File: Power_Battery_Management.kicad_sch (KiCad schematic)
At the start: 19 parts, among them J501 S2B-PH-SM4-TB, Q501 CSD85302L, U501 BQ29737DSER, U502 MCP73831T-2ACI/MC

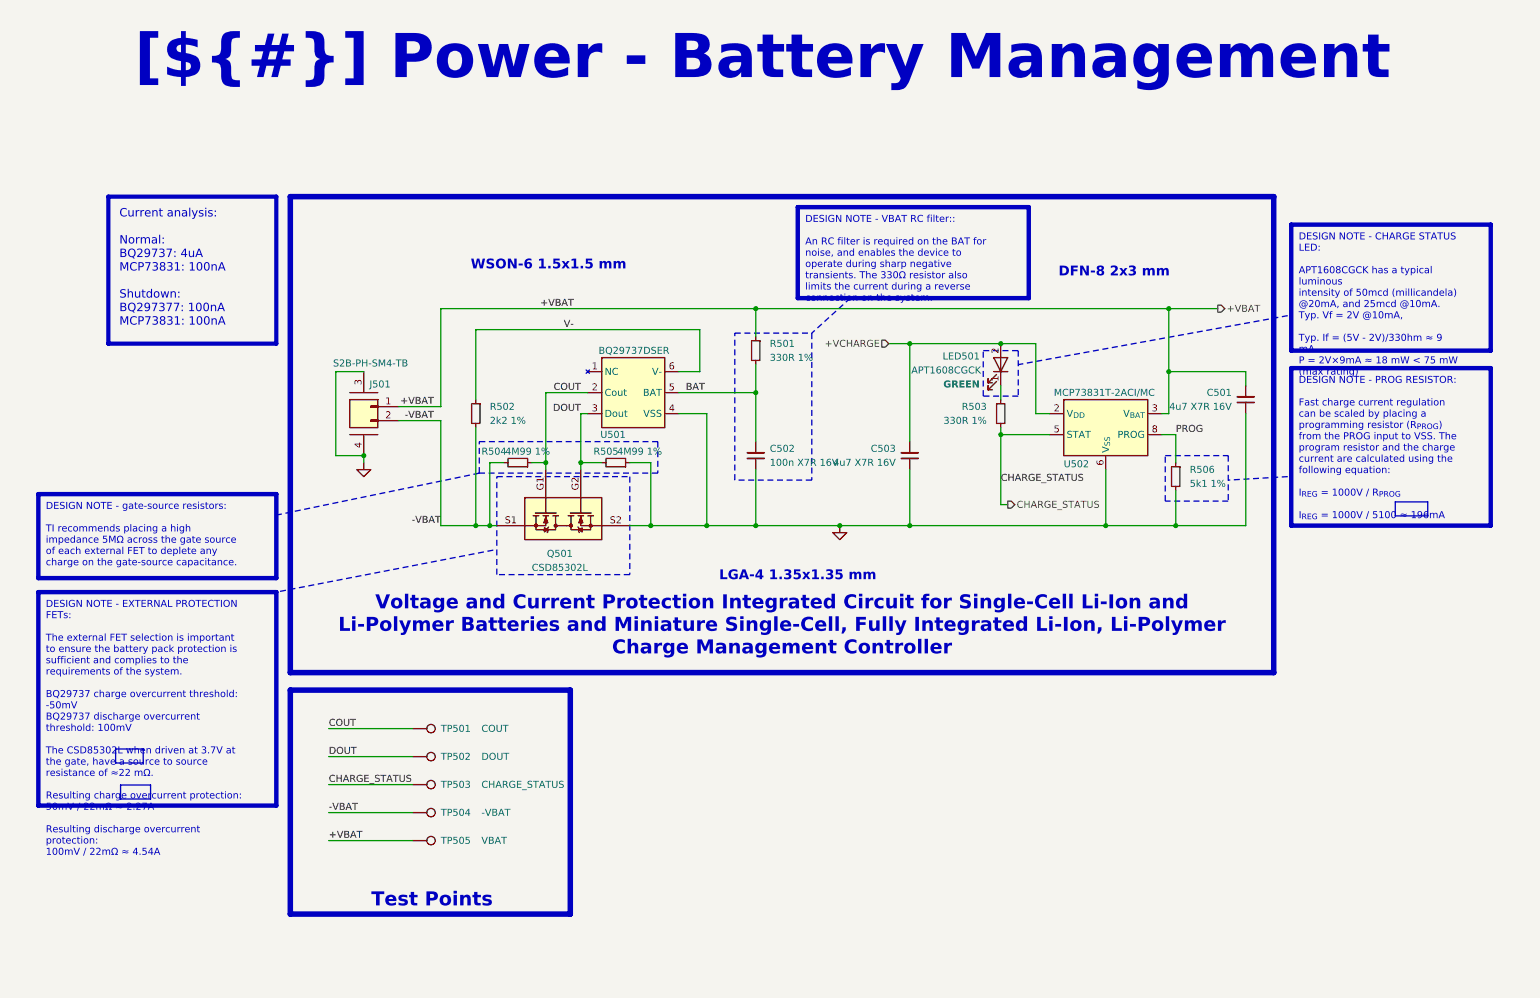
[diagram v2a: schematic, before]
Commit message: Finished schematic, imported all footprints, all 3D models and created STM32 project, now need to proofread shematic before layout
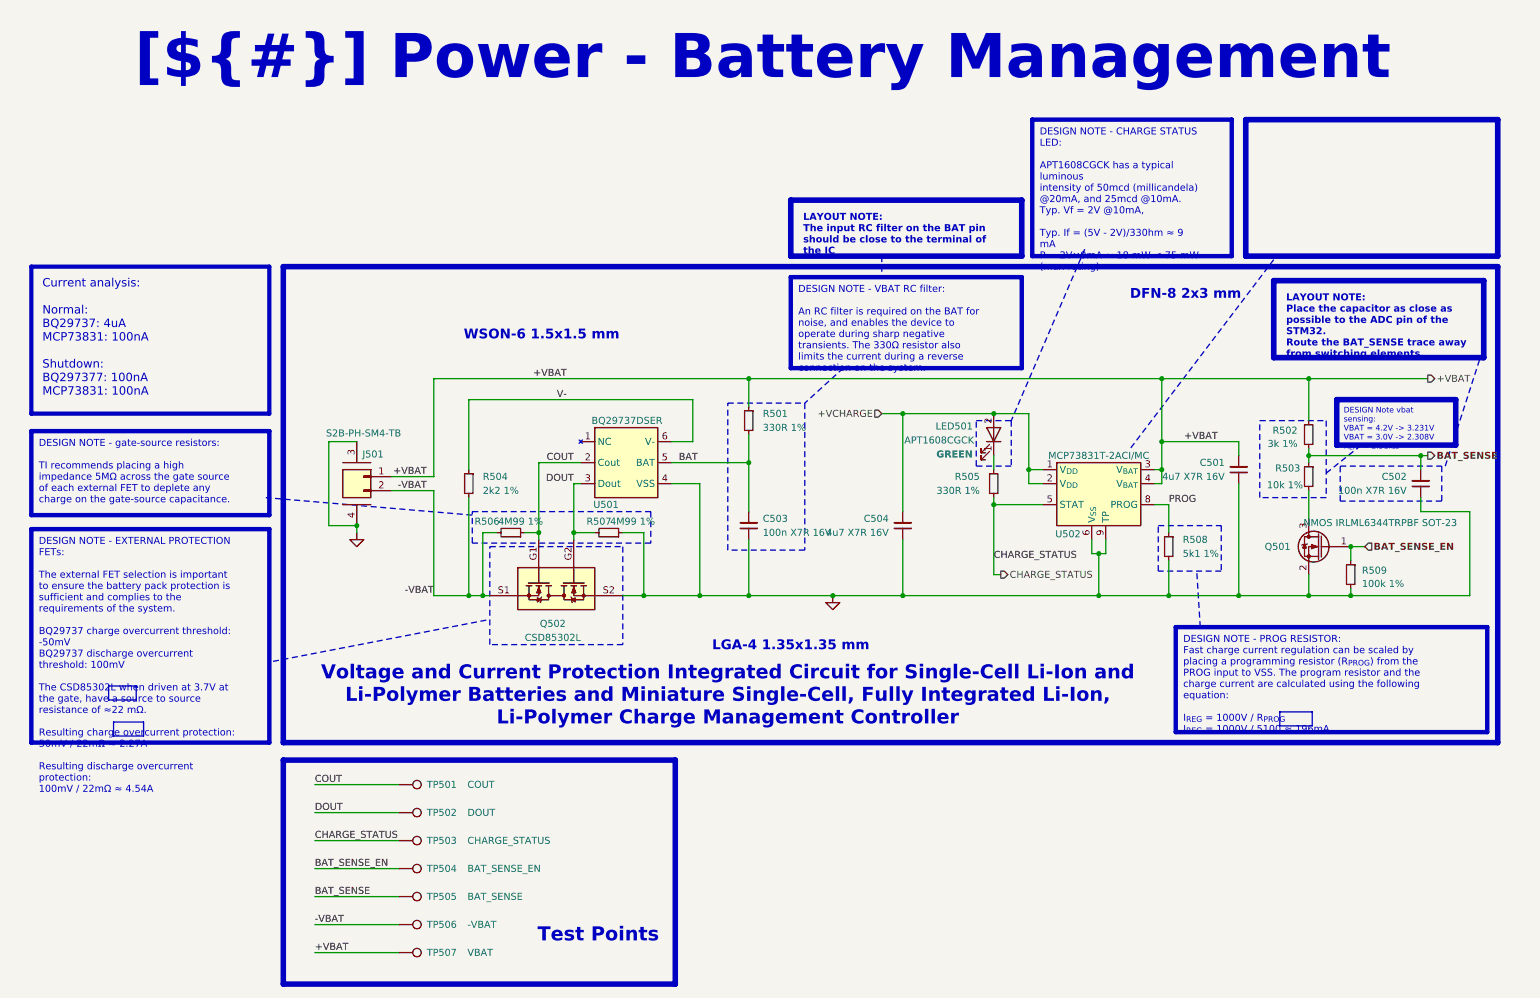
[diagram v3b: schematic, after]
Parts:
- added C502: 100n X7R 16V, Capacitor_SMD:C_0402_1005Metric, symbol Device:C_Small
- added Q501: NMOS IRLML6344TRPBF SOT-23, Package_TO_SOT_SMD:SOT-23, symbol Transistor_FET_Other:Q_NMOS_Depletion_GSD
- added R502: 3k 1%, Resistor_SMD:R_0402_1005Metric, symbol Device:R_Small
- added R503: 10k 1%, Resistor_SMD:R_0402_1005Metric, symbol Device:R_Small
- added R509: 100k 1%, Resistor_SMD:R_0402_1005Metric, symbol Device:R_Small
- added TP504: BAT_SENSE_EN, 0_Plume:TestPoint_Pad_D0.5mm_Back, symbol Connector:TestPoint
- added TP505: BAT_SENSE, 0_Plume:TestPoint_Pad_D0.5mm_Back, symbol Connector:TestPoint
- renumbered C502 to C503, C503 to C504, Q501 to Q502, R502 to R504, R503 to R505, R504 to R506, R505 to R507, R506 to R508, TP504 to TP506, TP505 to TP507
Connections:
- net +VBAT: now also R502.1
- net +VCHARGE: now also U502.1 (V_{DD})
- net GND: now also U502.9 (TP), C502.1, Q501.2 (S), R509.2
- new net: Q501.3 (D), R503.2
- new net BAT_SENSE: C502.2, R502.2, R503.1, TP505.1
- new net BAT_SENSE_EN: Q501.1 (G), R509.1, TP504.1
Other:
- moved on the sheet: C501, C503, C504, J501, LED501, Q502, R501, R504, R505, R506, R507, R508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

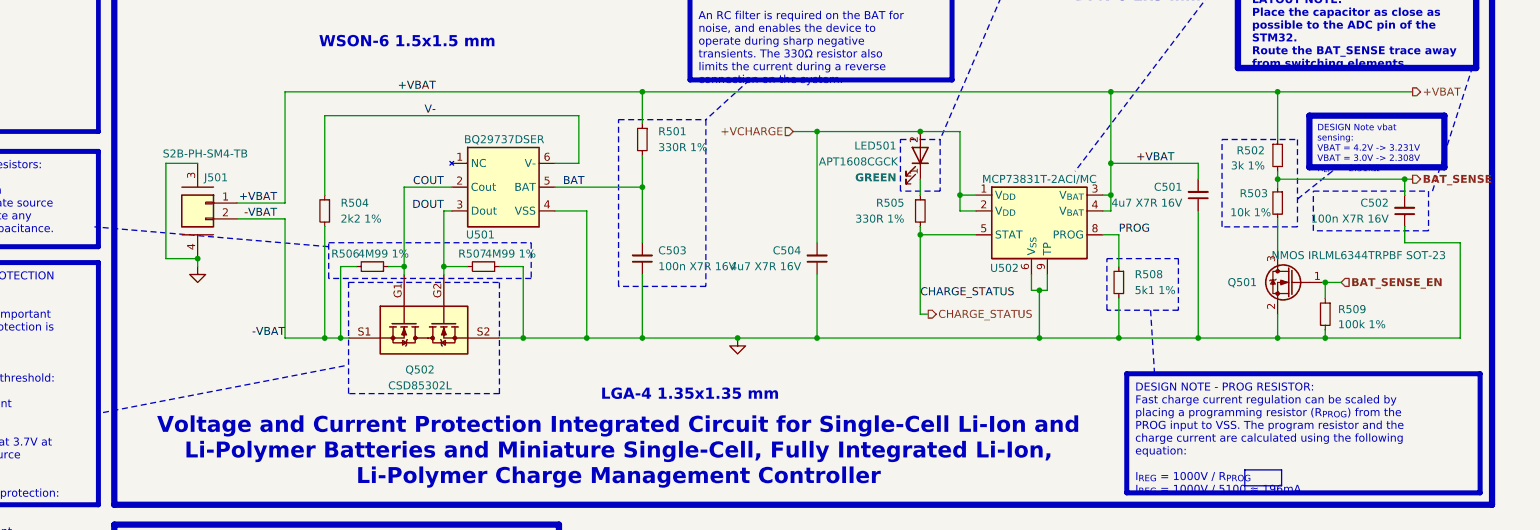
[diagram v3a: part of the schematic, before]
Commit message: Reviewed shematic, cleaned all DRC errors, chosed stackup, started layout
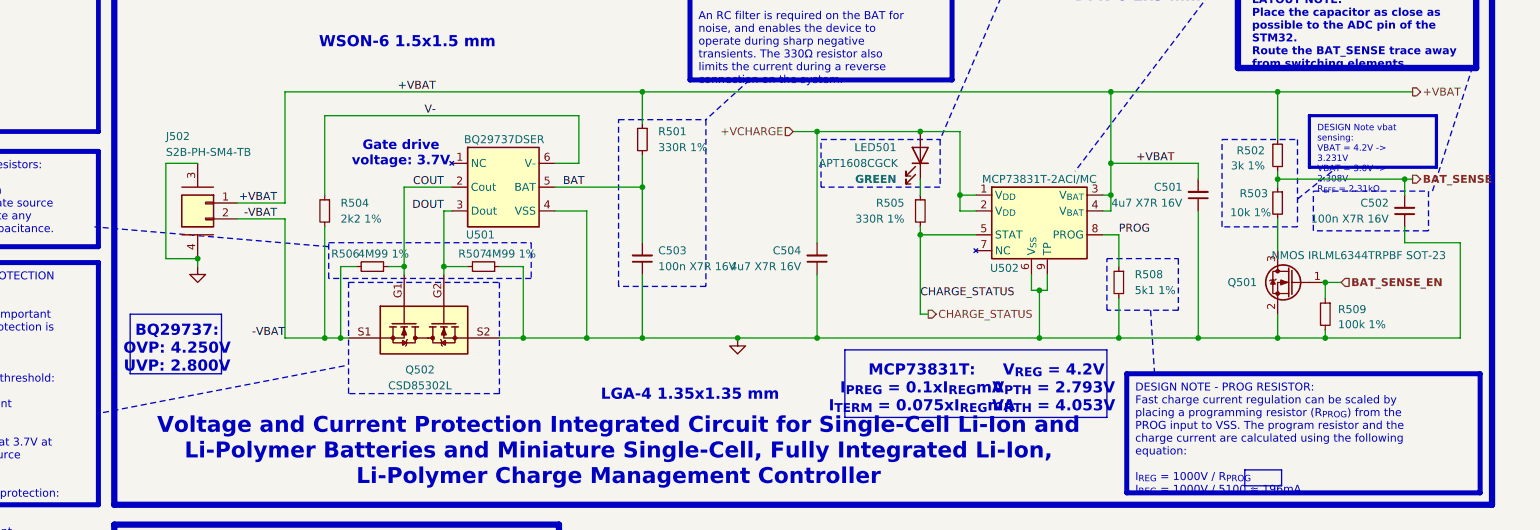
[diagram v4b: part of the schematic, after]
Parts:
- removed J501: S2B-PH-SM4-TB, 0_Plume:CONN_S2B-PH-SM4-TB_JST, symbol 0_connectors:Conn_01x02_Mounting
- added J502: S2B-PH-SM4-TB, 0_Plume:CONN_S2B-PH-SM4-TB_JST, symbol 0_Plume:CONN_S2B-PH-SM4-TB_JST
- LED501: symbol Charge_Manager_SYM:SM1206SRC -> Device:LED
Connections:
- net +VBAT: now also J502.1
- net -VBAT: now also J502.2
- net GND: now also J502.3, J502.4
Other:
- note added: "BQ29737: OVP: 4.250V UVP: 2.800V"
- note added: "Gate drive voltage: 3.7V"
- note added: "MCP73831T: I_{PREG} = 0.1xI_{REG}mA I_{TERM} = 0.075xI_{REG}mA"
- note added: "V_{REG} = 4.2V V_{PTH} = 2.793V V_{RTH} = 4.053V"

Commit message: Cleaned repo, cleaned and exported shematic, advanced rough layout
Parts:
- renumbered J502 to J501

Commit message: Advanced rough layout
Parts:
- added C506, C507: 47u X5R 16V, Capacitor_SMD:C_1206_3216Metric, symbol Device:C_Small
- added J405, J406: Solder Wire Pad 1,5x3mm, 0_Plume:SolderWirePad_SMD_1,5x3mm, symbol Connector_Generic:Conn_01x01
- R508: value 5k1 1% -> 2k2 1%; Manufacturer Part Number RK73H1ETTP5101F -> RK73H1ETTP2201F; Supplier Part Number 660-RK73H1ETTP5101F -> 660-RK73H1ETTP2201F
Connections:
- net +VBAT: now also C506.1, C507.2, J405.1 (Pin_1)
- net GND: now also C506.2, C507.1, J406.1 (Pin_1)
- net CHARGE_LED: now reaches LED501.1 (K), R505.1
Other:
- moved on the sheet: R505

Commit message: Finished layout, only cleaning left
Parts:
- added TP507, TP509: -VBAT, TestPoint:TestPoint_THTPad_D1.5mm_Drill0.7mm, symbol Connector:TestPoint
- J501: renamed from J405; footprint 0_Plume:SolderWirePad_SMD_1,5x3mm -> 0_Plume:Connector_SolderWirePad_SMD_1,5x3mm
- J503: renamed from J406; footprint 0_Plume:SolderWirePad_SMD_1,5x3mm -> 0_Plume:Connector_SolderWirePad_SMD_1,5x3mm
- LED501: footprint 0_Plume:KingBright_LED_0603 -> 0_Plume:LED_0603_KingBright
- TP508: renamed from TP507; value VBAT -> +VBAT
- renumbered C506 to C501, C507 to C502, C501 to C503, C502 to C504, C503 to C505, C504 to C506, J501 to J502
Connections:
- net +VBAT: now also TP509.1
- net -VBAT: now also J503.1 (Pin_1), TP507.1
- net GND: no longer J503.1 (Pin_1)
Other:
- moved on the sheet: J503, TP506, TP508
